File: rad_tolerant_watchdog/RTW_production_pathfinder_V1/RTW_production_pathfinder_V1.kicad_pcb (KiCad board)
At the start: 2 copper layers, 56 x 51 mm, 96 parts, among them J1 Breakout, J11 Breakout, J12 Breakout, J13 Breakout, J14 Breakout, J15 Breakout, J16 Breakout, J17 Breakout, J18 Breakout, U1 TLV1704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

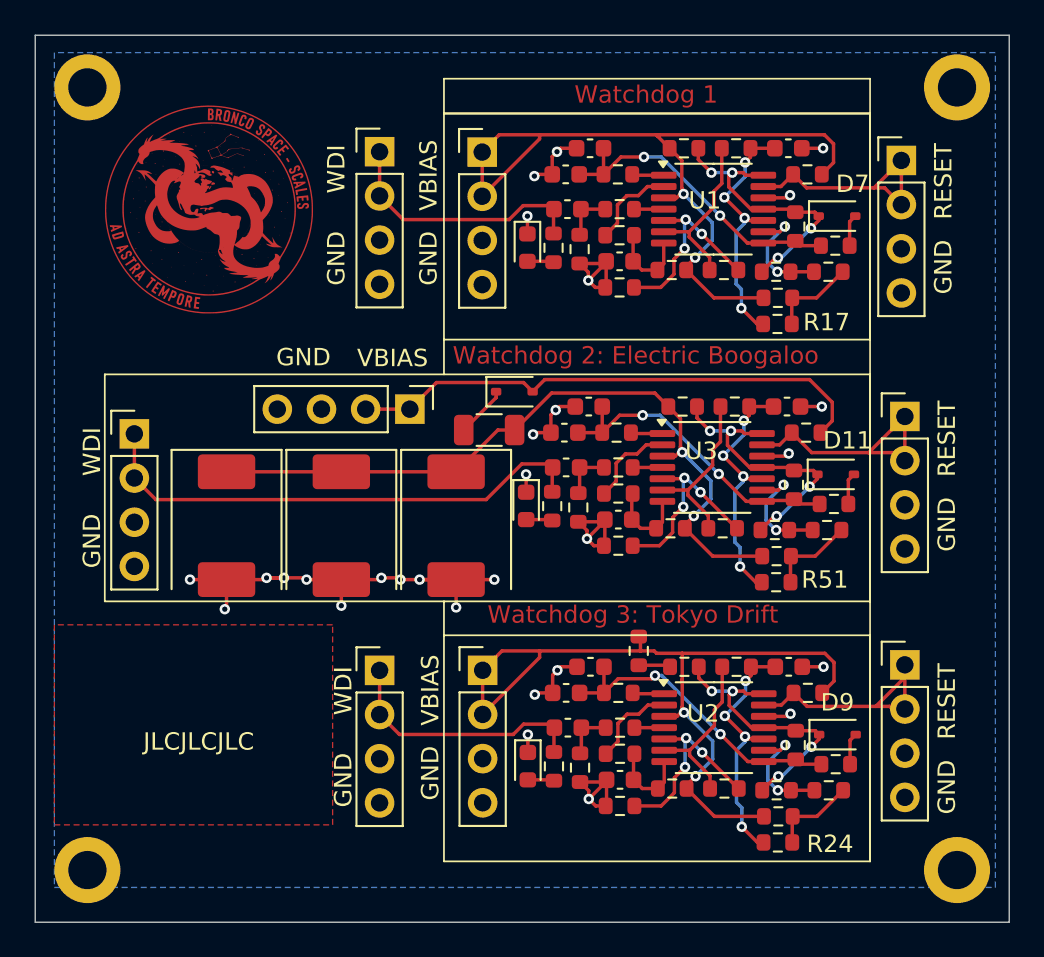
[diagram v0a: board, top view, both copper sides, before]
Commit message: Added Decoupling Caps on VBIAS
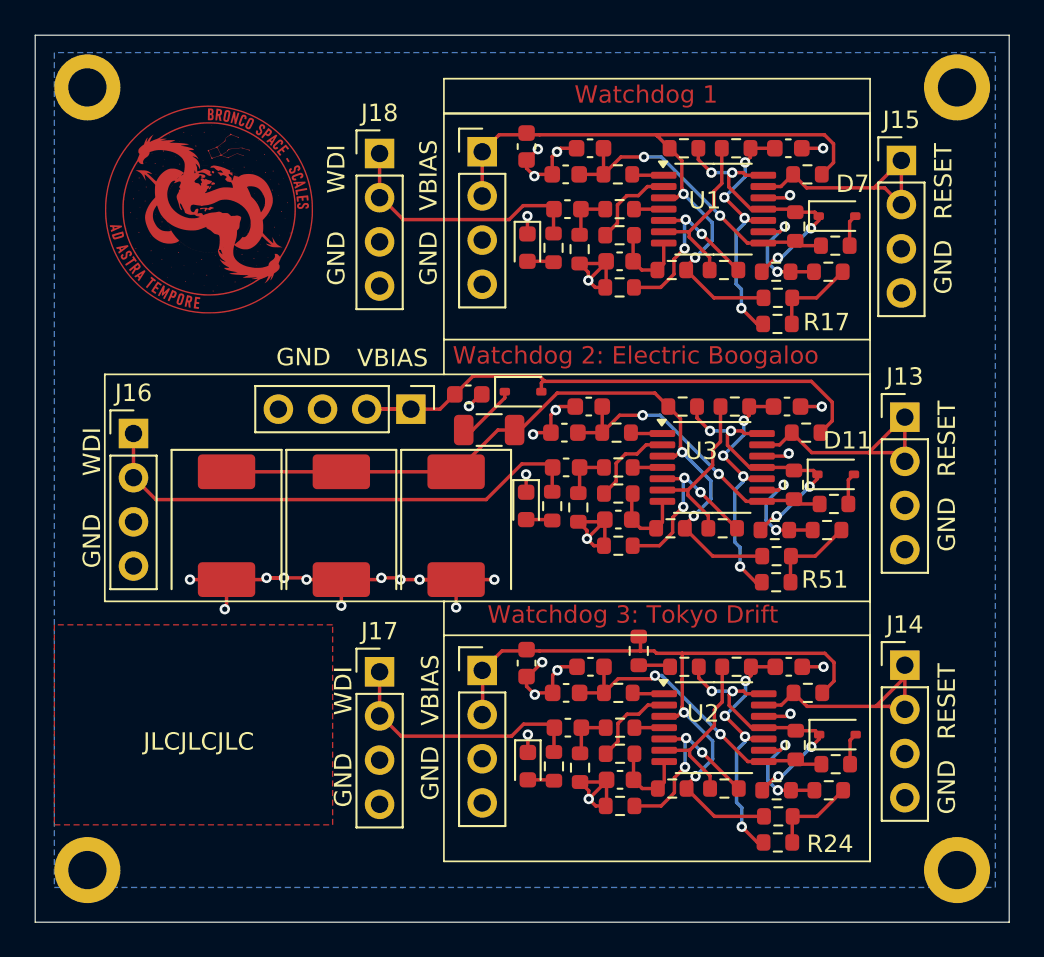
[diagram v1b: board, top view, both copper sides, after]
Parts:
- added C35: 10u, Capacitor_SMD:C_0603_1608Metric, F.Cu at (156.2, 83.4)
- added C36: 10u, Capacitor_SMD:C_0603_1608Metric, F.Cu at (156.2, 113.1)
- added C37: 10u, Capacitor_SMD:C_0603_1608Metric, F.Cu at (152.9, 97.7)
- J1: value Breakout -> VBIAS1 Input
- J11: value Breakout -> VBIAS3 Input
- J12: value Breakout -> VBIAS2 Input
- J13: value Breakout -> Watchdog 2 Output
- J14: value Breakout -> Watchdog 3 Output
- J15: value Breakout -> Watchdog 1 Output
- J16: value Breakout -> Watchdog 2 Input
- J17: value Breakout -> Watchdog 3 Input
- J18: value Breakout -> Watchdog 1 Input
- moved D5 0.50 mm to (156.1, 97.5)
- moved J18 0.10 mm to (147.8, 83.8)
- moved J17 0.08 mm to (147.8, 113.6)
- moved J12 0.06 mm to (149.6, 98.5)
- moved J16 0.05 mm to (133.7, 99.9)
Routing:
- net GND: track 69.1 -> 74.6 mm, vias 29 -> 32
- net VBIAS_3: track 47.1 -> 42.1 mm
- net VBIAS_1: track 46.7 -> 41.8 mm
- net VBIAS_2: track 30.5 -> 33.5 mm
- net Net-(D5-Pad1): track 2.98 -> 3.48 mm

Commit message: Added Bypass Caps to WDT 1 & 2
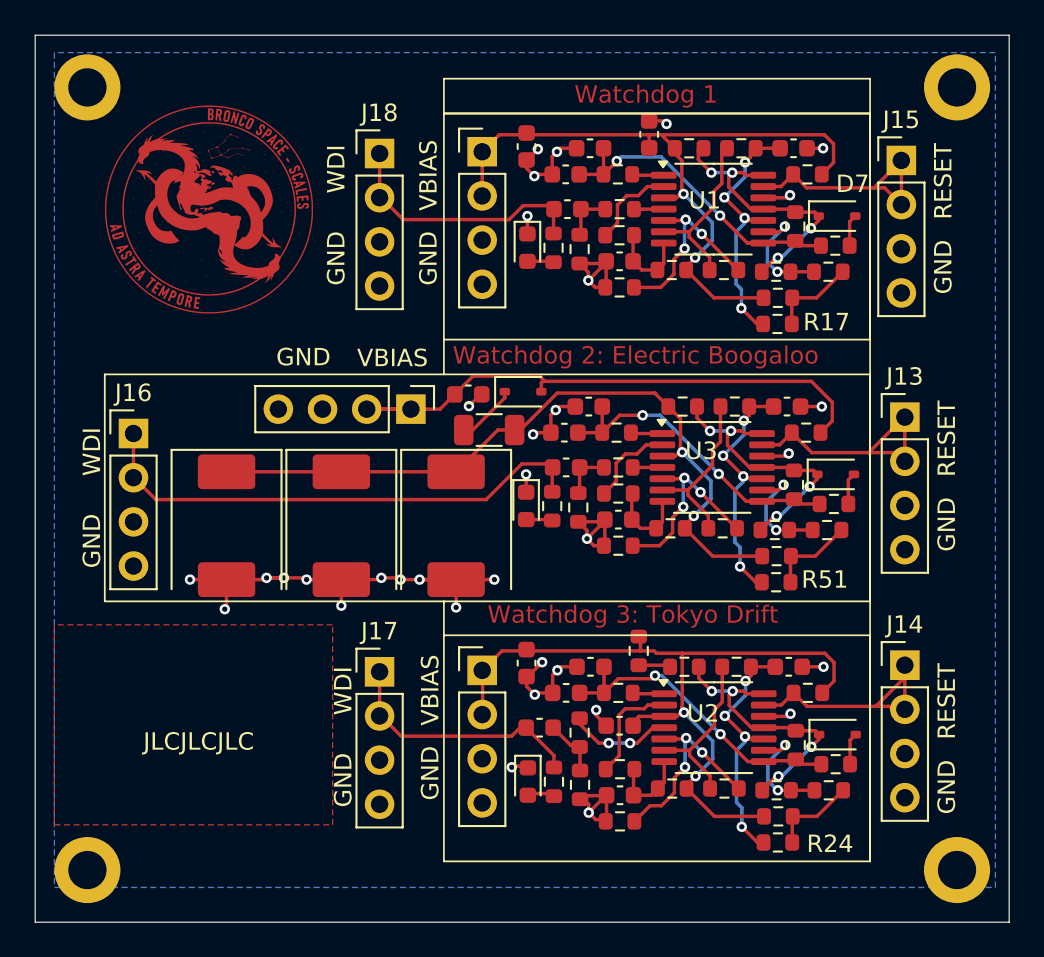
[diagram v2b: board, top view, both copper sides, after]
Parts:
- added C38: 10u, Capacitor_SMD:C_0603_1608Metric, F.Cu at (163.3, 82.7)
- added C39: 10u, Capacitor_SMD:C_0603_1608Metric, F.Cu at (161.6, 116.7)
- moved R40 2.34 mm to (159.3, 117.1), turned to 90 degrees
- moved C25 1.62 mm to (157.0, 116.8)
- moved R39 0.99 mm to (159.3, 120.1)
- moved C26 0.89 mm to (161.6, 120.7)
- moved R27 0.89 mm to (161.6, 122.2)
- moved R38 0.89 mm to (157.8, 119.9)
- moved R41 0.89 mm to (161.6, 119.2)
- moved D8 0.89 mm to (156.3, 119.9)
- moved C24 0.30 mm to (171.6, 83.5)
- moved R18 0.30 mm to (168.6, 83.5)
- moved R36 0.30 mm to (165.6, 83.5)
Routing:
- net Net-(U2A--): track 1.71 -> 6.11 mm, vias 0 -> 2
- net GND: track 74.6 -> 76.6 mm, vias 32 -> 34
- net VBIAS_3: track 42.1 -> 43.9 mm
- net Net-(R41-Pad1): track 5.13 -> 6.27 mm

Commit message: Updated RTW Production Files Mar 18 2025
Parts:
- moved C29 11.2 mm to (167.3, 123.8), turned to 0 degrees
- moved C34 11.0 mm to (167.4, 108.7), turned to 0 degrees
- moved C24 10.8 mm to (167.6, 93.5), turned to 0 degrees
- moved R25 9.01 mm to (167.7, 122.3)
- moved R52 8.88 mm to (167.5, 107.2)
- moved R18 8.56 mm to (167.6, 92.0)
- moved R27 3.00 mm to (164.6, 121.8)
- moved R20 2.45 mm to (164.0, 92.0)
- moved R54 2.34 mm to (163.8, 106.9)
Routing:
- net GND: track 76.6 -> 68.5 mm, vias 34 -> 39
- net Net-(U1D--): track 14.8 -> 10.1 mm, vias 4 -> 2
- net Net-(U1B--): track 9.73 -> 5.46 mm
- net Net-(U2D--): track 14.8 -> 10.8 mm, vias 4 -> 2
- net Net-(U3B--): track 9.73 -> 5.83 mm
- net Net-(U2B--): track 9.73 -> 5.99 mm
- net Net-(U3D--): track 14.8 -> 11.2 mm, vias 4 -> 2
- net VBIAS_3: track 43.9 -> 41.7 mm, vias 2 -> 3
- net VBIAS_1: track 42.2 -> 40.5 mm, vias 2 -> 3
- net VBIAS_2: track 33.5 -> 31.9 mm
- net /Watchdog3/WDT-VP: track 11.9 -> 10.6 mm, vias 3 -> 2
- net /Watchdog2/WDT-VP: track 11.5 -> 10.3 mm, vias 3 -> 2
- net /Watchdog1/WDT-VP: track 11.5 -> 10.4 mm, vias 3 -> 2
- net Net-(U1D-+): track 16.3 -> 15.8 mm, vias 4 -> 2
- net Net-(U3D-+): track 16.3 -> 16.0 mm, vias 4 -> 2
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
